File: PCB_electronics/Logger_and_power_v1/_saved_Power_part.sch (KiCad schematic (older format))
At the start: 21 parts, among them IC1 ATMEGA328-P, P1 SOLAR_PANEL, P2 5V_pololu, P3 BATT, P4 SUPERCAPS, U1 IRLB_8721_SOL, U2 IRLS-8721_MEGA, Y1 16MHz

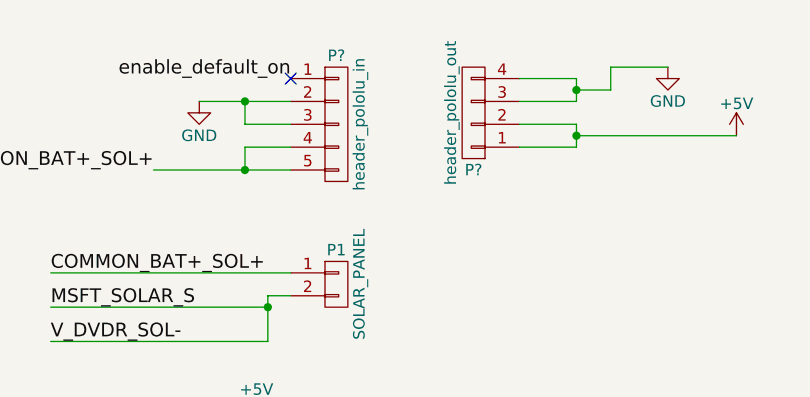
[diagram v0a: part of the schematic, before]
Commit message: now pololu on PCB; need to export gerbers still
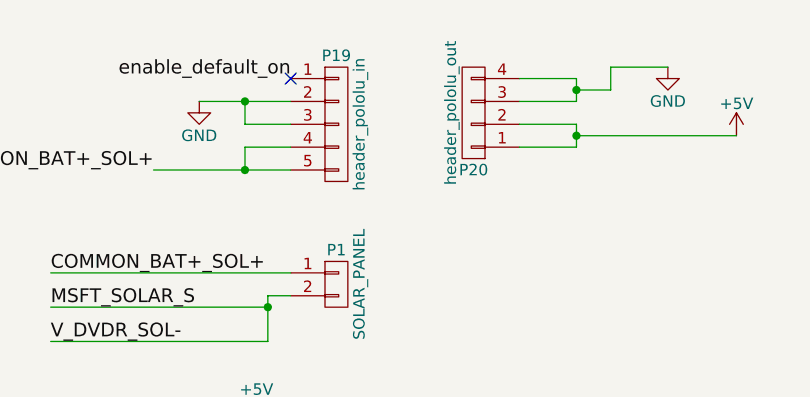
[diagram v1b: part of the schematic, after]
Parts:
- P19: renamed from P?; footprint (none) -> Pin_Headers:Pin_Header_Straight_1x05
- P20: renamed from P?; footprint (none) -> Pin_Headers:Pin_Header_Straight_1x04
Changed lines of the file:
@@
 NoConn ~ 10200 3750
 $Comp
-L CONN_01X05 P?
+L CONN_01X05 P19
 U 1 1 5D40578E
 P 8150 950
-F 0 "P?" H 8150 1250 50  0000 C CNN
+F 0 "P19" H 8150 1250 50  0000 C CNN
 F 1 "header_pololu_in" V 8250 950 50  0000 C CNN
-F 2 "" H 8150 950 50  0000 C CNN
+F 2 "Pin_Headers:Pin_Header_Straight_1x05" H 8150 950 50  0001 C CNN
 F 3 "" H 8150 950 50  0000 C CNN
 	1    8150 950
@@
 $EndComp
 $Comp
-L CONN_01X04 P?
+L CONN_01X04 P20
 U 1 1 5D405903
 P 8750 900
-F 0 "P?" H 8750 1150 50  0000 C CNN
+F 0 "P20" H 8750 1150 50  0000 C CNN
 F 1 "header_pololu_out" V 8850 900 50  0000 C CNN
-F 2 "" H 8750 900 50  0000 C CNN
+F 2 "Pin_Headers:Pin_Header_Straight_1x04" H 8750 900 50  0001 C CNN
 F 3 "" H 8750 900 50  0000 C CNN
 	1    8750 900
@@
 Connection ~ 9200 1000
 $Comp
-L GND #PWR?
+L GND #PWR019
 U 1 1 5D405E2B
 P 9600 700
-F 0 "#PWR?" H 9600 450 50  0001 C CNN
+F 0 "#PWR019" H 9600 450 50  0001 C CNN
 F 1 "GND" H 9600 550 50  0000 C CNN
 F 2 "" H 9600 700 50  0000 C CNN
@@
 	9350 700  9600 700
 $Comp
-L +5V #PWR?
+L +5V #PWR020
 U 1 1 5D406012
 P 9900 1000
-F 0 "#PWR?" H 9900 850 50  0001 C CNN
+F 0 "#PWR020" H 9900 850 50  0001 C CNN
 F 1 "+5V" H 9900 1140 50  0000 C CNN
 F 2 "" H 9900 1000 50  0000 C CNN
@@
 Connection ~ 7750 850
 $Comp
-L GND #PWR?
+L GND #PWR021
 U 1 1 5D406578
 P 7550 850
-F 0 "#PWR?" H 7550 600 50  0001 C CNN
+F 0 "#PWR021" H 7550 600 50  0001 C CNN
 F 1 "GND" H 7550 700 50  0000 C CNN
 F 2 "" H 7550 850 50  0000 C CNN
